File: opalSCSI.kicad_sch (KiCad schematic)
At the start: 79 parts, among them J1 Amphenol L717SDB25PA4CH3R, J2 PGM, J3 Micro_SD_Card, J4 USB_B_Micro, SW1 RST, U1 STM32F103CBTx, U2 LT1117-3.3, Y1 8Mhz, Y2 CM7V-T1A-32.768k-9pF-20PPM-TA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

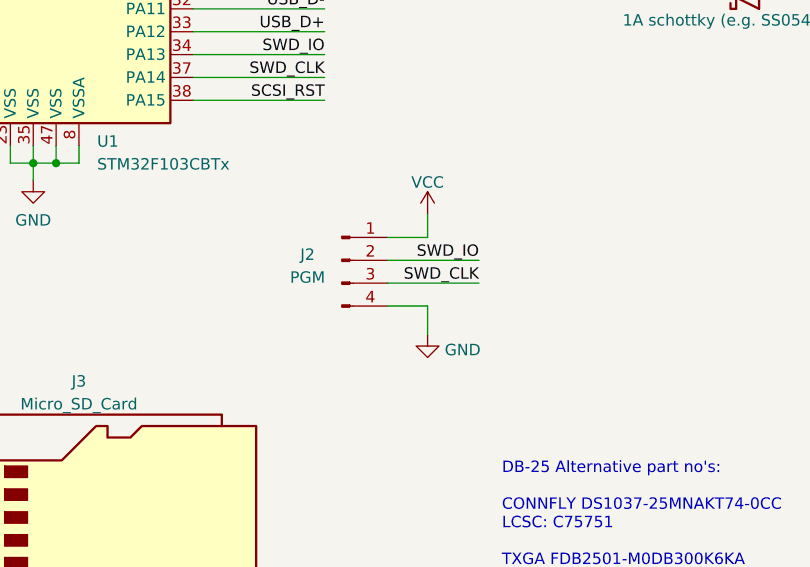
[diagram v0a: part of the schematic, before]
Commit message: Add nReset pin to programming (SWD) header
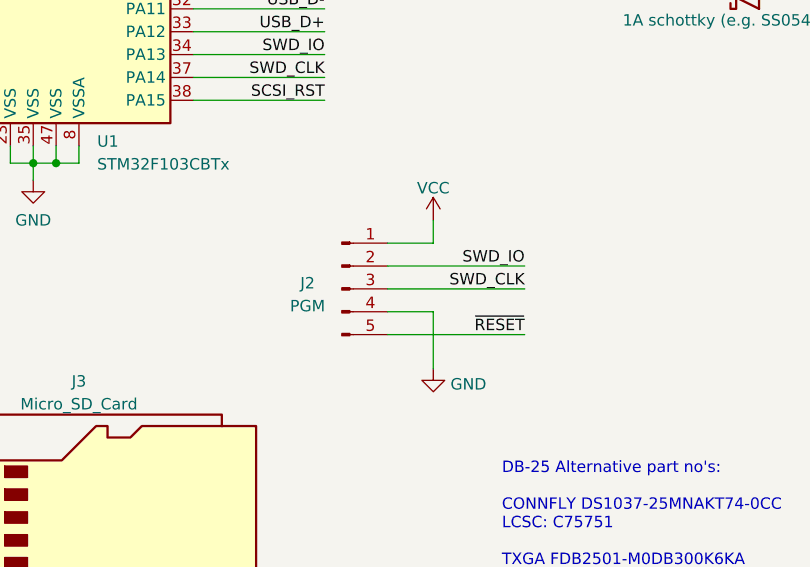
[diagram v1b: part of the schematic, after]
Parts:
- J2: footprint Connector_PinHeader_2.54mm:PinHeader_1x04_P2.54mm_Vertical -> Connector_PinHeader_2.54mm:PinHeader_1x05_P2.54mm_Vertical; symbol Connector:Conn_01x04_Male -> Connector:Conn_01x05_Male
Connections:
- net ~{RESET}: now also J2.5 (Pin_5)
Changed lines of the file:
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@@
     (stroke (width 0) (type default) (color 0 0 0 0))
   )
-  (wire (pts (xy 182.88 123.825) (xy 187.325 123.825))
+  (wire (pts (xy 182.88 124.46) (xy 187.96 124.46))
     (stroke (width 0) (type default) (color 0 0 0 0))
   )
@@
     (stroke (width 0) (type default) (color 0 0 0 0))
   )
-  (wire (pts (xy 182.88 121.285) (xy 193.04 121.285))
-    (stroke (width 0) (type default) (color 0 0 0 0))
-  )
   (wire (pts (xy 140.97 107.95) (xy 143.51 107.95))
     (stroke (width 0) (type default) (color 0 0 0 0))
@@
     (stroke (width 0) (type default) (color 0 0 0 0))
   )
-  (wire (pts (xy 182.88 118.745) (xy 193.04 118.745))
-    (stroke (width 0) (type default) (color 0 0 0 0))
-  )
   (wire (pts (xy 266.7 52.07) (xy 266.7 68.58))
     (stroke (width 0) (type default) (color 0 0 0 0))
@@
     (stroke (width 0) (type default) (color 0 0 0 0))
   )
+  (wire (pts (xy 182.88 121.92) (xy 198.12 121.92))
+    (stroke (width 0) (type default) (color 0 0 0 0))
+  )
   (wire (pts (xy 83.185 34.29) (xy 83.185 39.37))
     (stroke (width 0) (type default) (color 0 0 0 0))
@@
     (stroke (width 0) (type default) (color 0 0 0 0))
   )
+  (wire (pts (xy 182.88 119.38) (xy 198.12 119.38))
+    (stroke (width 0) (type default) (color 0 0 0 0))
+  )
   (wire (pts (xy 247.015 68.58) (xy 247.015 59.69))
     (stroke (width 0) (type default) (color 0 0 0 0))
   )
+  (wire (pts (xy 182.88 127) (xy 198.12 127))
+    (stroke (width 0) (type default) (color 0 0 0 0))
+  )
   (wire (pts (xy 255.27 92.075) (xy 234.315 92.075))
     (stroke (width 0) (type default) (color 0 0 0 0))
@@
     (stroke (width 0) (type default) (color 0 0 0 0))
   )
-  (wire (pts (xy 187.325 116.205) (xy 187.325 113.665))
+  (wire (pts (xy 187.96 116.84) (xy 187.96 114.3))
     (stroke (width 0) (type default) (color 0 0 0 0))
   )
@@
     (stroke (width 0) (type default) (color 0 0 0 0))
   )
-  (wire (pts (xy 182.88 116.205) (xy 187.325 116.205))
+  (wire (pts (xy 182.88 116.84) (xy 187.96 116.84))
     (stroke (width 0) (type default) (color 0 0 0 0))
   )
@@
     (stroke (width 0) (type default) (color 0 0 0 0))
   )
-  (wire (pts (xy 187.325 123.825) (xy 187.325 127))
+  (wire (pts (xy 187.96 124.46) (xy 187.96 130.81))
     (stroke (width 0) (type default) (color 0 0 0 0))
   )
@@
     (effects (font (size 1.27 1.27)) (justify left bottom))
   )
-  (label "SWD_IO" (at 193.04 118.745 180)
+  (label "SWD_IO" (at 198.12 119.38 180)
     (effects (font (size 1.27 1.27)) (justify right bottom))
   )
@@
     (effects (font (size 1.27 1.27)) (justify right bottom))
   )
+  (label "~{RESET}" (at 198.12 127 180)
+    (effects (font (size 1.27 1.27)) (justify right bottom))
+  )
   (label "SCSI_SEL" (at 234.315 120.015 0)
     (effects (font (size 1.27 1.27)) (justify left bottom))
@@
     (effects (font (size 1.27 1.27)) (justify right bottom))
   )
-  (label "SWD_CLK" (at 193.04 121.285 180)
+  (label "SWD_CLK" (at 198.12 121.92 180)
     (effects (font (size 1.27 1.27)) (justify right bottom))
   )
@@
     (pin "2")
   )
-  (symbol (lib_id "Connector:Conn_01x04_Male") (at 177.8 118.745 0) (unit 1)
+  (symbol (lib_id "Connector:Conn_01x05_Male") (at 177.8 121.92 0) (unit 1)
     (in_bom yes) (on_board yes)
-    (property "Reference" "J2" (id 0) (at 173.99 118.11 0))
-    (property "Value" "PGM" (id 1) (at 173.99 120.65 0))
-    (property "Footprint" "Connector_PinHeader_2.54mm:PinHeader_1x04_P2.54mm_Vertical" (id 2) (at 177.8 118.745 0)
+    (property "Reference" "J2" (id 0) (at 173.99 121.285 0))
+    (property "Value" "PGM" (id 1) (at 173.99 123.825 0))
+    (property "Footprint" "Connector_PinHeader_2.54mm:PinHeader_1x05_P2.54mm_Vertical" (id 2) (at 177.8 121.92 0)
       (effects (font (size 1.27 1.27)) hide)
     )
-    (property "Datasheet" "~" (id 3) (at 177.8 118.745 0)
+    (property "Datasheet" "~" (id 3) (at 177.8 121.92 0)
       (effects (font (size 1.27 1.27)) hide)
     )
@@
     (pin "3")
     (pin "4")
+    (pin "5")
   )
   (symbol (lib_id "Mechanical:MountingHole_Pad") (at 71.755 180.975 0) (unit 1)
@@
     (pin "1")
   )
-  (symbol (lib_id "power:GND") (at 187.325 127 0) (unit 1)
+  (symbol (lib_id "power:GND") (at 187.96 130.81 0) (unit 1)
     (in_bom yes) (on_board yes) (fields_autoplaced)
-    (property "Reference" "#PWR024" (id 0) (at 187.325 133.35 0)
+    (property "Reference" "#PWR024" (id 0) (at 187.96 137.16 0)
       (effects (font (size 1.27 1.27)) hide)
     )
-    (property "Value" "GND" (id 1) (at 189.23 128.7038 0)
+    (property "Value" "GND" (id 1) (at 189.865 132.5138 0)
       (effects (font (size 1.27 1.27)) (justify left))
     )
-    (property "Footprint" "" (id 2) (at 187.325 127 0)
+    (property "Footprint" "" (id 2) (at 187.96 130.81 0)
       (effects (font (size 1.27 1.27)) hide)
     )
-    (property "Datasheet" "" (id 3) (at 187.325 127 0)
+    (property "Datasheet" "" (id 3) (at 187.96 130.81 0)
       (effects (font (size 1.27 1.27)) hide)
     )
@@
     (pin "2")
   )
-  (symbol (lib_id "power:VCC") (at 187.325 113.665 0) (unit 1)
+  (symbol (lib_id "power:VCC") (at 187.96 114.3 0) (unit 1)
     (in_bom yes) (on_board yes) (fields_autoplaced)
-    (property "Reference" "#PWR019" (id 0) (at 187.325 117.475 0)
+    (property "Reference" "#PWR019" (id 0) (at 187.96 118.11 0)
       (effects (font (size 1.27 1.27)) hide)
     )
-    (property "Value" "VCC" (id 1) (at 187.325 110.0892 0))
-    (property "Footprint" "" (id 2) (at 187.325 113.665 0)
+    (property "Value" "VCC" (id 1) (at 187.96 110.7242 0))
+    (property "Footprint" "" (id 2) (at 187.96 114.3 0)
       (effects (font (size 1.27 1.27)) hide)
     )
-    (property "Datasheet" "" (id 3) (at 187.325 113.665 0)
+    (property "Datasheet" "" (id 3) (at 187.96 114.3 0)
       (effects (font (size 1.27 1.27)) hide)
     )
@@
     )
     (path "/197569cf-4f4f-4db4-b99b-34626873de70"
-      (reference "J2") (unit 1) (value "PGM") (footprint "Connector_PinHeader_2.54mm:PinHeader_1x04_P2.54mm_Vertical")
+      (reference "J2") (unit 1) (value "PGM") (footprint "Connector_PinHeader_2.54mm:PinHeader_1x05_P2.54mm_Vertical")
     )
     (path "/f268b3ee-c0c5-4b08-87ad-2f0a66d42c3b"
